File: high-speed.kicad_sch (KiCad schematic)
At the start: 2 parts, among them J301 245863050104829+

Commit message: essential routing done
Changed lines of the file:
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@@
 	(wire
 		(pts
-			(xy 250.19 90.17) (xy 273.05 90.17)
+			(xy 250.19 90.17) (xy 260.35 90.17)
 		)
 		(stroke
@@
 	(label "DSI0_DATA.0_P"
 		(at 90.17 128.27 0)
+		(fields_autoplaced yes)
 		(effects
 			(font
@@
 	(label "DSI0_CLK.N"
 		(at 90.17 140.97 0)
+		(fields_autoplaced yes)
 		(effects
 			(font
@@
 	(label "LED_PWR.PWM"
 		(at 252.73 102.87 0)
+		(fields_autoplaced yes)
 		(effects
 			(font
@@
 	(label "DSI0_DATA.1_N"
 		(at 90.17 133.35 0)
+		(fields_autoplaced yes)
 		(effects
 			(font
@@
 	(label "DSI0_DATA.2_N"
 		(at 90.17 148.59 0)
+		(fields_autoplaced yes)
 		(effects
 			(font
@@
 	(label "DSI0_DATA.3_P"
 		(at 15.24 151.13 0)
+		(fields_autoplaced yes)
 		(effects
 			(font
@@
 	(label "DSI0_DATA.1_P"
 		(at 90.17 135.89 0)
+		(fields_autoplaced yes)
 		(effects
 			(font
@@
 	(label "DSI0_DATA.2_P"
 		(at 90.17 151.13 0)
+		(fields_autoplaced yes)
 		(effects
 			(font
@@
 	(label "DSI0_DATA.3_N"
 		(at 15.24 148.59 0)
+		(fields_autoplaced yes)
 		(effects
 			(font
@@
 	(label "DSI0_DATA.0_N"
 		(at 90.17 125.73 0)
+		(fields_autoplaced yes)
 		(effects
 			(font
@@
 	(label "DSI0_CLK.P"
 		(at 90.17 143.51 0)
+		(fields_autoplaced yes)
 		(effects
 			(font
@@
 	(symbol
 		(lib_id "power:GND")
-		(at 273.05 90.17 90)
+		(at 260.35 90.17 90)
 		(unit 1)
 		(exclude_from_sim no)
@@
 		(fields_autoplaced yes)
 		(property "Reference" "#PWR0313"
-			(at 279.4 90.17 0)
+			(at 266.7 90.17 0)
 			(effects
 				(font
@@
 		)
 		(property "Value" "GND"
-			(at 276.86 90.1699 90)
+			(at 264.16 90.1699 90)
 			(effects
 				(font
@@
 		)
 		(property "Footprint" ""
-			(at 273.05 90.17 0)
+			(at 260.35 90.17 0)
 			(effects
 				(font
@@
 		)
 		(property "Datasheet" ""
-			(at 273.05 90.17 0)
+			(at 260.35 90.17 0)
 			(effects
 				(font
@@
 		)
 		(property "Description" "Power symbol creates a global label with name \"GND\" , ground"
-			(at 273.05 90.17 0)
-			(effects
-				(font
+			(at 260.35 90.17 0)
+			(effects
+				(font

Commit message: more routing
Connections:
- net DSI0_DATA.3_P: no longer Module301.196 (DSI1_D3_P)
- net GND: now also Module301.107 (GND), Module301.108 (GND), Module301.113 (GND), Module301.114 (GND), Module301.119 (GND), Module301.120 (GND), Module301.125 (GND), Module301.126 (GND), Module301.131 (GND), Module301.132 (GND), Module301.137 (GND), Module301.138 (GND), Module301.144 (GND), Module301.150 (GND), Module301.155 (GND), Module301.156 (GND), Module301.161 (GND), Module301.162 (GND), Module301.167 (GND), Module301.168 (GND), Module301.173 (GND), Module301.174 (GND), Module301.179 (GND), Module301.180 (GND), Module301.185 (GND), Module301.186 (GND), Module301.191 (GND), Module301.192 (GND), Module301.197 (GND), Module301.198 (GND)
- net CAM1_D0_N: now reaches Module301.115 (CAM1_D0_N)
- net CAM1_D0_P: now reaches Module301.117 (CAM1_D0_P)
- net CAM1_D1_N: now reaches Module301.121 (CAM1_D1_N)
- net CAM1_D1_P: now reaches Module301.123 (CAM1_D1_P)
- net CAM1_C_N: now reaches Module301.127 (CAM1_C_N)
- net CAM1_C_P: now reaches Module301.129 (CAM1_C_P)
- net CAM1_D2_N: now reaches Module301.133 (CAM1_D2_N)
- net CAM1_D2_P: now reaches Module301.135 (CAM1_D2_P)
- net CAM1_D3_N: now reaches Module301.139 (CAM1_D3_N)
- net CAM1_D3_P: now reaches Module301.141 (CAM1_D3_P)
- net HDMI1_HOTPLUG: now reaches Module301.143 (HDMI1_HOTPLUG)
- net HDMI1_SDA: now reaches Module301.145 (HDMI1_SDA)
- net HDMI1_D2_P: now reaches Module301.146 (HDMI1_TX2_P)
- net HDMI1_SCL: now reaches Module301.147 (HDMI1_SCL)
- net HDMI1_D2_N: now reaches Module301.148 (HDMI1_TX2_N)
- net HDMI1_CEC: now reaches Module301.149 (HDMI1_CEC)
- net HDMI0_CEC: now reaches Module301.151 (HDMI0_CEC)
- net HDMI1_D1_P: now reaches Module301.152 (HDMI1_TX1_P)
- net HDMI0_HOTPLUG: now reaches Module301.153 (HDMI0_HOTPLUG)
- net HDMI1_D1_N: now reaches Module301.154 (HDMI1_TX1_N)
- net HDMI1_D0_P: now reaches Module301.158 (HDMI1_TX0_P)
- net HDMI1_D0_N: now reaches Module301.160 (HDMI1_TX0_N)
- net HDMI1_CK_P: now reaches Module301.164 (HDMI1_CLK_P)
- net HDMI1_CK_N: now reaches Module301.166 (HDMI1_CLK_N)
- net HDMI0_D2_P: now reaches Module301.170 (HDMI0_TX2_P)
- net HDMI0_D2_N: now reaches Module301.172 (HDMI0_TX2_N)
- net HDMI0_D1_P: now reaches Module301.176 (HDMI0_TX1_P)
- net HDMI0_D1_N: now reaches Module301.178 (HDMI0_TX1_N)
- net HDMI0_D0_P: now reaches Module301.182 (HDMI0_TX0_P)
- net HDMI0_D0_N: now reaches Module301.184 (HDMI0_TX0_N)
- net HDMI0_CK_P: now reaches Module301.188 (HDMI0_CLK_P)
- net HDMI0_CK_N: now reaches Module301.190 (HDMI0_CLK_N)
- net HDMI0_SDA: now reaches Module301.199 (HDMI0_SDA)
- net HDMI0_SCL: now reaches Module301.200 (HDMI0_SCL)
- no-connect marks 10 -> 24
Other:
- note added: "Display Mezzaine"
- moved on the sheet: J301, Module301B

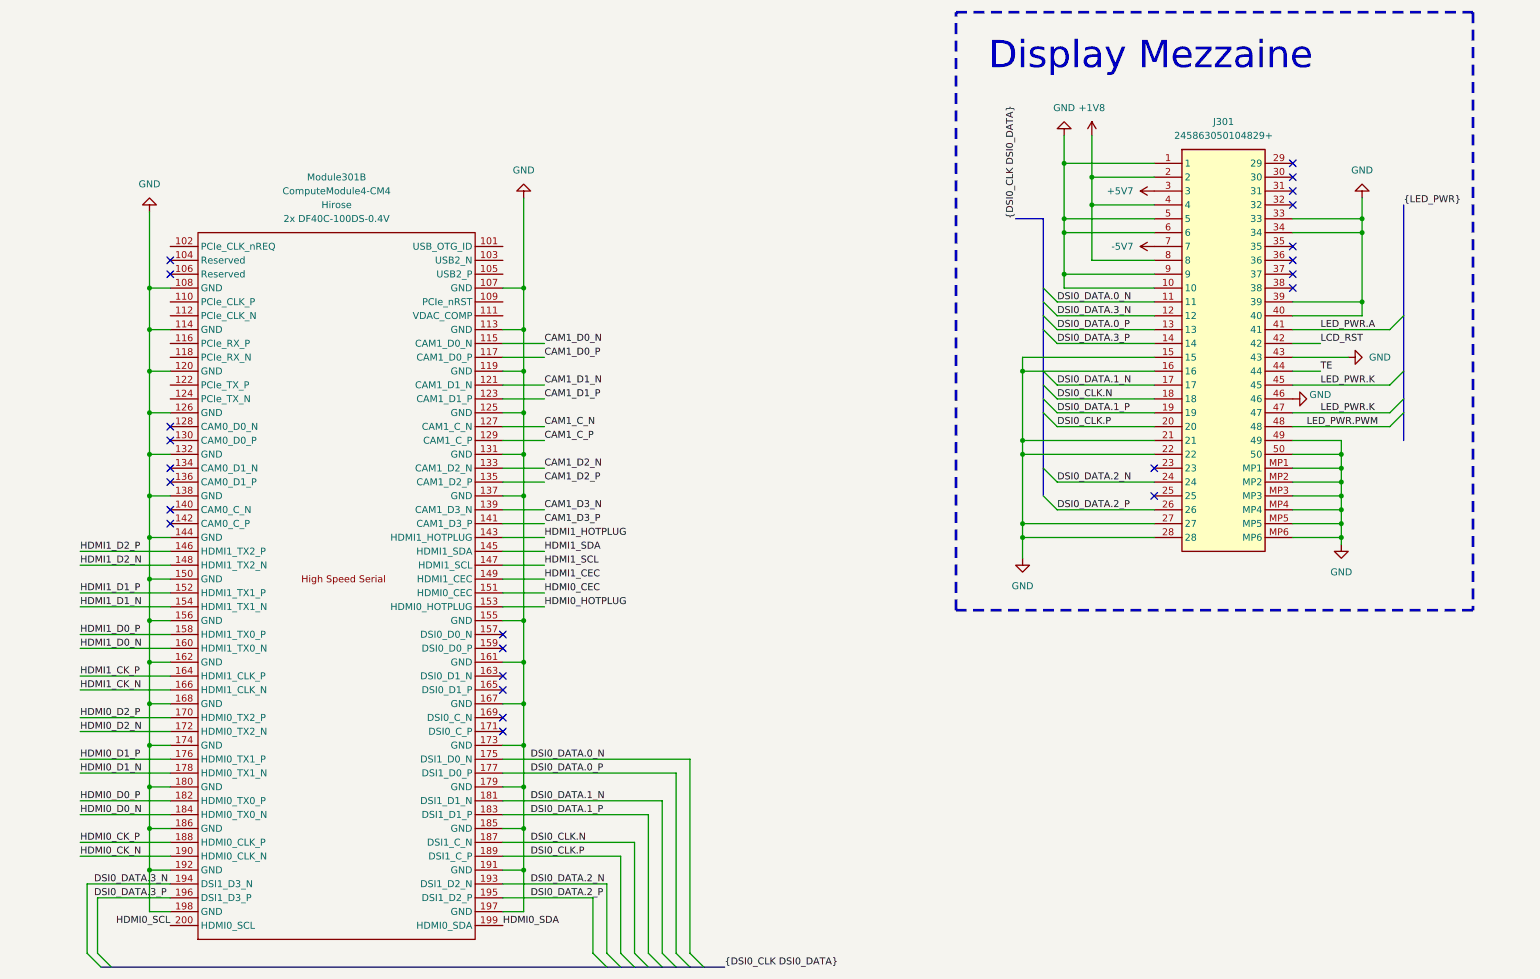
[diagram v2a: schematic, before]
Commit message: 1v8 buck and 4.7uh inductor
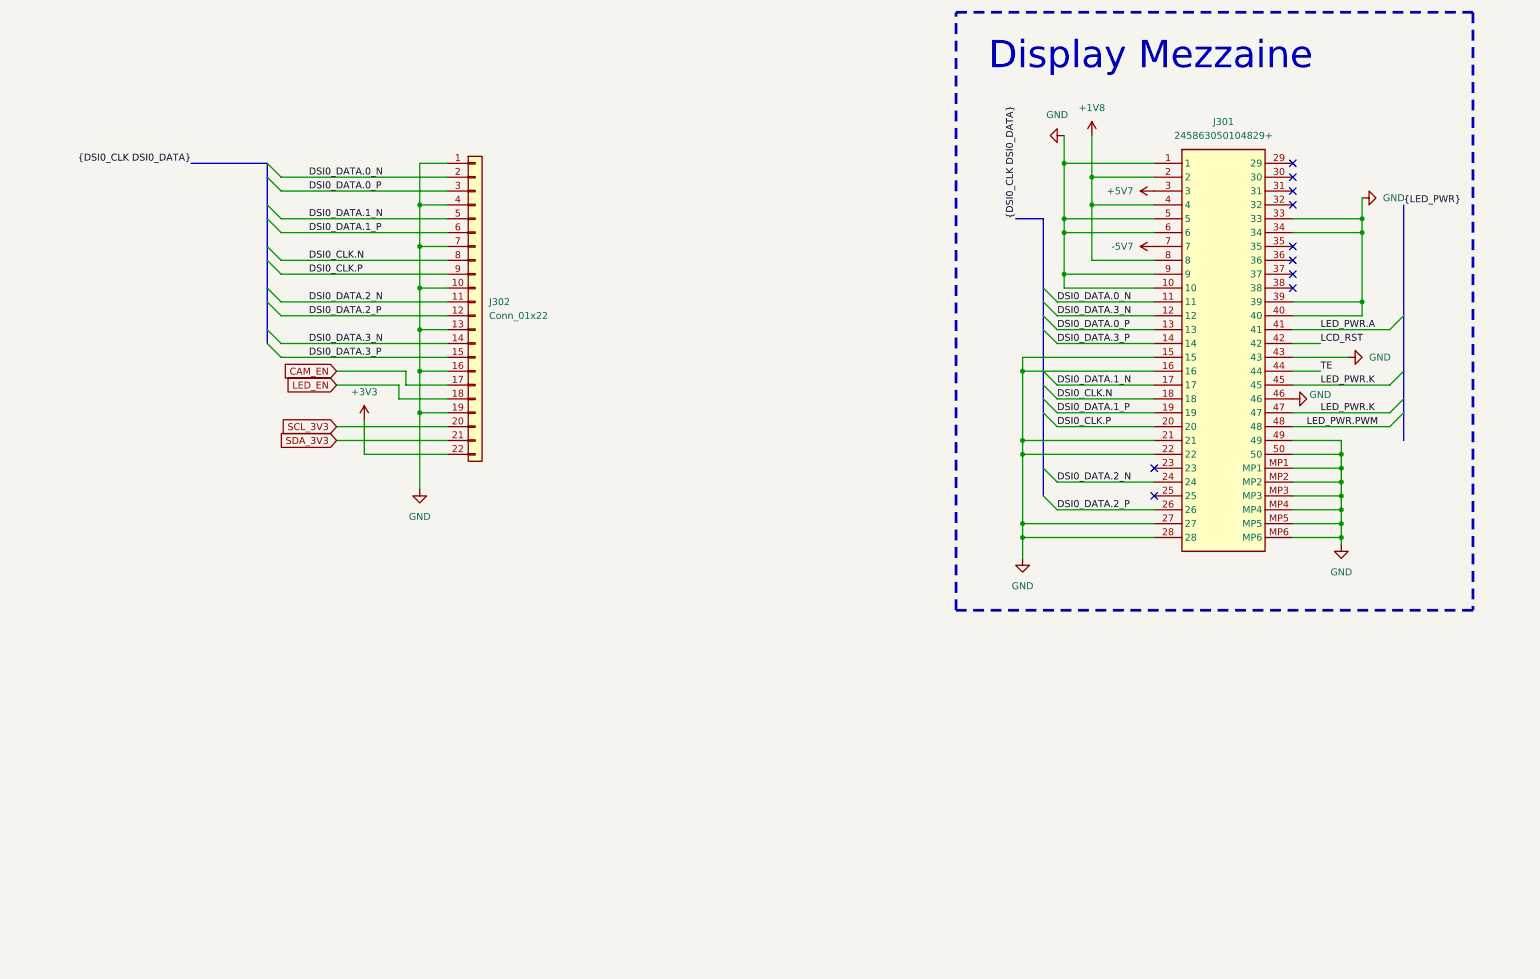
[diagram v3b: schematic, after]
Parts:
- removed Module301: ComputeModule4-CM4, CM4IO:Raspberry-Pi-4-Compute-Module, symbol CM4IO:ComputeModule4-CM4
- added J302: Conn_01x22, footprints:CON22_1X22_DRB_XF2C_TYC, symbol Connector_Generic:Conn_01x22
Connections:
- net DSI0_CLK.N: now also J302.8 (Pin_8)
- net DSI0_CLK.P: now also J302.9 (Pin_9)
- net DSI0_DATA.0_N: now also J302.2 (Pin_2)
- net DSI0_DATA.0_P: now also J302.3 (Pin_3)
- net DSI0_DATA.1_N: now also J302.5 (Pin_5)
- net DSI0_DATA.1_P: now also J302.6 (Pin_6)
- net DSI0_DATA.2_N: now also J302.11 (Pin_11)
- net DSI0_DATA.2_P: now also J302.12 (Pin_12)
- net DSI0_DATA.3_N: now also J302.14 (Pin_14)
- net DSI0_DATA.3_P: now also J302.15 (Pin_15)
- net GND: now also J302.1 (Pin_1), J302.10 (Pin_10), J302.13 (Pin_13), J302.16 (Pin_16), J302.19 (Pin_19), J302.4 (Pin_4), J302.7 (Pin_7)
- new net +3V3: J302.22 (Pin_22)
- new net CAM_EN: J302.17 (Pin_17)
- new net LED_EN: J302.18 (Pin_18)
- new net SCL_3V3: J302.20 (Pin_20)
- new net SDA_3V3: J302.21 (Pin_21)
- no-connect marks 24 -> 10

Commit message: init layout
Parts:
- added J303: Conn_01x02_LCD_Breakout, Connector_PinHeader_2.54mm:PinHeader_1x02_P2.54mm_Vertical, symbol Connector:Conn_01x02_Pin
- added J304: Conn_01x04_power_jumpers, Connector_PinHeader_2.54mm:PinHeader_1x04_P2.54mm_Vertical, symbol Connector:Conn_01x04_Pin
- J301: footprint 245863050104829 -> footprints:245863050104829_missing pads; symbol 245863050104829+:245863050104829+ -> 245863050104829+:245863050104829+_missing_gnd
- J302: footprint footprints:CON22_1X22_DRB_XF2C_TYC -> CON22_1X22_DRB_XF2C_TYC; symbol Connector_Generic:Conn_01x22 -> XF2M-2215-1A:XF2M-2215-1A
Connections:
- net +3V3: now also J304.3 (Pin_3), J304.4 (Pin_4)
- net GND: now also J302.23 (Pin_23_case), J302.24 (Pin_24_case), J304.1 (Pin_1), J304.2 (Pin_2)
- net LCD_RST: now also J303.1 (Pin_1); no longer J301.42
- net TE: now also J303.2 (Pin_2)
- net CAM_EN renamed LCD_RESET
- net LCD_RESET: now also J301.42
- net LED_EN renamed LED_PWM

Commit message: board fabbed
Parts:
- removed J303: Conn_01x02_LCD_Breakout, Connector_PinHeader_2.54mm:PinHeader_1x02_P2.54mm_Vertical, symbol Connector:Conn_01x02_Pin
- added H305, H307, H308: MountingHole_Pad, MountingHole:MountingHole_3.2mm_M3_DIN965_Pad_TopBottom, symbol Mechanical:MountingHole_Pad
- added J305: Conn_01x03_Pin, Connector_PinHeader_2.54mm:PinHeader_1x03_P2.54mm_Vertical, symbol Connector:Conn_01x03_Pin
- added R301, R302, R303: 2.2kΩ, Resistor_SMD:R_0402_1005Metric, symbol Device:R
- added R304: 2.7kΩ, Resistor_SMD:R_0603_1608Metric, symbol Device:R
- J302: footprint CON22_1X22_DRB_XF2C_TYC -> footprints:CON22_1X22_DRB_XF2C_TYC
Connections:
- net +1V8: now also J304.3 (Pin_3), J304.4 (Pin_4)
- net +3V3: now also R301.1, R302.1; no longer J304.3 (Pin_3), J304.4 (Pin_4)
- net GND: now also H305.1, H307.1, H308.1, R304.2
- net LCD_RESET: now also R303.1; no longer J301.42
- net SCL_3V3: now also R301.2
- net SDA_3V3: now also R302.2
- net TE: now also J305.2 (Pin_2)
- net LED_PWR.PWM renamed LCD_CONNECTOR_PWM
- net LCD_CONNECTOR_PWM: now also J305.3 (Pin_3)
- new net LCD_RESET_DISPLAY_SIDE: J301.42, J305.1 (Pin_1), R303.2, R304.1

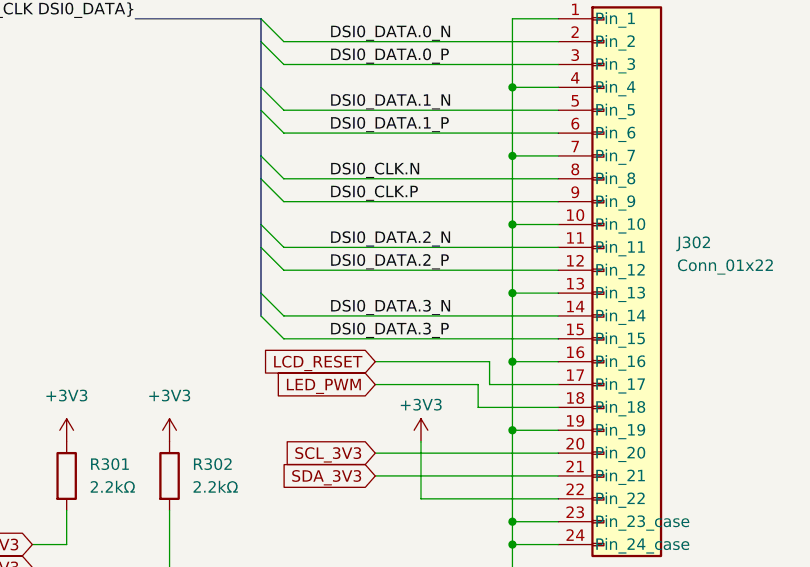
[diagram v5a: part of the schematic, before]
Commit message: better driver design now that the cm5 has pin swapping support
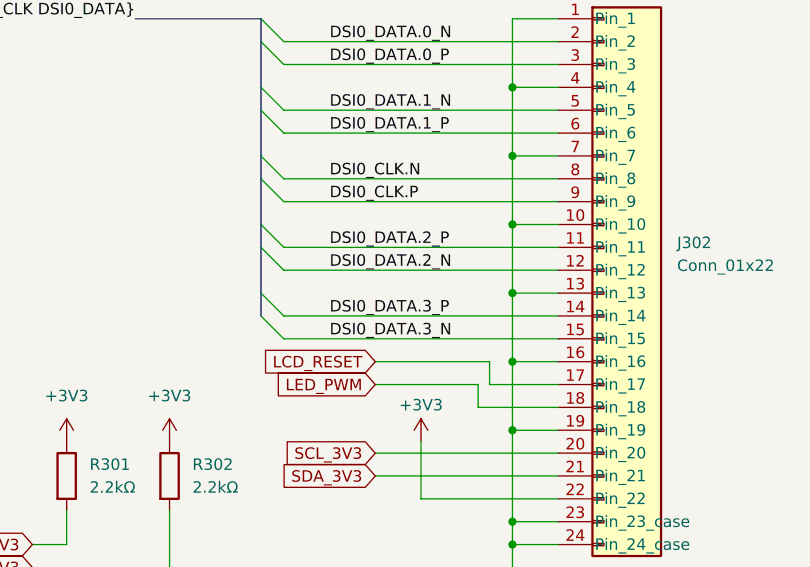
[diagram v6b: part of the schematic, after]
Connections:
- net DSI0_DATA.2_N: now also J302.12 (Pin_12); no longer J302.11 (Pin_11)
- net DSI0_DATA.2_P: now also J302.11 (Pin_11); no longer J302.12 (Pin_12)
- net DSI0_DATA.3_N: now also J302.15 (Pin_15); no longer J302.14 (Pin_14)
- net DSI0_DATA.3_P: now also J302.14 (Pin_14); no longer J302.15 (Pin_15)
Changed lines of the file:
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@@
-		)
-	)
-	(label "DSI0_DATA.3_P"
-		(at 116.84 80.01 0)
-		(effects
-			(font
-				(size 1.27 1.27)
-			)
-			(justify left bottom)
-		)
-	)
-	(label "DSI0_DATA.2_N"
-		(at 116.84 69.85 0)
-		(effects
-			(font
-				(size 1.27 1.27)
-			)
-			(justify left bottom)
 		)
 	)
@@
 		)
 	)
-	(label "DSI0_DATA.2_P"
-		(at 116.84 72.39 0)
-		(effects
-			(font
-				(size 1.27 1.27)
-			)
-			(justify left bottom)
-		)
-	)
 	(label "DSI0_DATA.0_N"
 		(at 116.84 46.99 0)
@@
 		)
 	)
-	(label "DSI0_DATA.3_N"
-		(at 116.84 77.47 0)
+	(label "DSI0_DATA.2_P"
+		(at 116.84 69.85 0)
 		(effects
 			(font
@@
 	(label "DSI0_DATA.1_N"
 		(at 204.47 83.82 0)
+		(effects
+			(font
+				(size 1.27 1.27)
+			)
+			(justify left bottom)
+		)
+	)
+	(label "DSI0_DATA.2_N"
+		(at 116.84 72.39 0)
+		(effects
+			(font
+				(size 1.27 1.27)
+			)
+			(justify left bottom)
+		)
+	)
+	(label "DSI0_DATA.3_N"
+		(at 116.84 80.01 0)
 		(effects
 			(font
@@
 		(effects
 			(font
+				(size 1.27 1.27)
+			)
+			(justify left bottom)
+		)
+	)
+	(label "DSI0_DATA.3_P"
+		(at 116.84 77.47 0)
+		(effects
+			(font
